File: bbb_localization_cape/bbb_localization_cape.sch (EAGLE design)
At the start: 33 parts, among them J2 MOLEX-22-03-5035, U1 SN65HVD256DR, U2 ARDUCAMOV5642, U3 SN74LV1T126DCKR, U4 MSP430G2553IPW20R, U5 SN74LV1T125DCKR, U6 LP38693MP-3.3/NOPB, U7 LM1085ISX-ADJ

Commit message: Went over the entire schematic
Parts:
- removed C1: 100nF, resistor:C-USC1206
- removed R3: 47k, resistor:R-US_R1206
- J2: device bbb_cape_parts:MOLEX-22-03-5035 -> bbb_localization_cape:MOLEX-22-03-5035
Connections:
- removed net N$7: C1.1, R3.1, U4.P1.3/ADC10CLK/CAOUT/VREF-/VEREF-/A3/CA3
- net +3V3: no longer R3.2
- net GND: no longer C1.2
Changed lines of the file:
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@@
 <setting verticaltext="up"/>
 </settings>
-<grid distance="0.1" unitdist="inch" unit="inch" style="lines" multiple="1" display="yes" altdistance="0.01" altunitdist="inch" altunit="inch"/>
+<grid distance="0.1" unitdist="inch" unit="inch" style="lines" multiple="1" display="no" altdistance="0.01" altunitdist="inch" altunit="inch"/>
 <layers>
 <layer number="1" name="Top" color="4" fill="1" visible="no" active="no"/>
@@
 <part name="U4" library="bbb_cape_parts" deviceset="MSP430G2553IPW20R" device=""/>
 <part name="+3V35" library="supply1" library_urn="urn:adsk.eagle:library:371" deviceset="+3V3" device=""/>
-<part name="R3" library="resistor" library_urn="urn:adsk.eagle:library:348" deviceset="R-US_" device="R1206" package3d_urn="urn:adsk.eagle:package:26062/1" value="47k"/>
-<part name="C1" library="resistor" library_urn="urn:adsk.eagle:library:348" deviceset="C-US" device="C1206" package3d_urn="urn:adsk.eagle:package:26140/1" value="100nF"/>
-<part name="GND3" library="supply1" library_urn="urn:adsk.eagle:library:371" deviceset="GND" device=""/>
 <part name="+3V37" library="supply1" library_urn="urn:adsk.eagle:library:371" deviceset="+3V3" device=""/>
 <part name="R5" library="resistor" library_urn="urn:adsk.eagle:library:348" deviceset="R-US_" device="R1206" package3d_urn="urn:adsk.eagle:package:26062/1" value="47k"/>
@@
 <part name="R4" library="resistor" library_urn="urn:adsk.eagle:library:348" deviceset="R-US_" device="R1206" package3d_urn="urn:adsk.eagle:package:26062/1" value="10k"/>
 <part name="P+4" library="supply1" library_urn="urn:adsk.eagle:library:371" deviceset="+5V" device=""/>
-<part name="J2" library="bbb_cape_parts" deviceset="MOLEX-22-03-5035" device=""/>
+<part name="J2" library="bbb_localization_cape" deviceset="MOLEX-22-03-5035" device=""/>
 <part name="GND6" library="supply1" library_urn="urn:adsk.eagle:library:371" deviceset="GND" device=""/>
 <part name="SUPPLY1" library="supply2" library_urn="urn:adsk.eagle:library:372" deviceset="+10V" device=""/>
@@
 <attribute name="VALUE" x="65.7606" y="92.9386" size="2.0828" layer="96" ratio="6" rot="SR0"/>
 </instance>
-<instance part="+3V35" gate="G$1" x="20.32" y="96.52" smashed="yes">
-<attribute name="VALUE" x="20.32" y="96.52" size="1.778" layer="96"/>
-</instance>
-<instance part="R3" gate="G$1" x="20.32" y="83.82" smashed="yes" rot="R90">
-<attribute name="NAME" x="23.9014" y="85.09" size="1.778" layer="95"/>
-<attribute name="VALUE" x="23.622" y="82.55" size="1.778" layer="96"/>
-</instance>
-<instance part="C1" gate="G$1" x="20.32" y="71.12" smashed="yes">
-<attribute name="NAME" x="23.876" y="69.215" size="1.778" layer="95"/>
-<attribute name="VALUE" x="23.876" y="66.929" size="1.778" layer="96"/>
-</instance>
-<instance part="GND3" gate="1" x="20.32" y="60.96"/>
+<instance part="+3V35" gate="G$1" x="55.88" y="91.44" smashed="yes">
+<attribute name="VALUE" x="55.88" y="91.44" size="1.778" layer="96"/>
+</instance>
 <instance part="+3V37" gate="G$1" x="256.54" y="93.98" smashed="yes">
 <attribute name="VALUE" x="256.54" y="93.98" size="1.778" layer="96"/>
@@
 </busses>
 <nets>
-<net name="N$7" class="0">
-<segment>
-<pinref part="R3" gate="G$1" pin="1"/>
-<wire x1="20.32" y1="78.74" x2="20.32" y2="76.2" width="0.1524" layer="91"/>
-<pinref part="U4" gate="A" pin="P1.3/ADC10CLK/CAOUT/VREF-/VEREF-/A3/CA3"/>
-<wire x1="20.32" y1="76.2" x2="58.42" y2="76.2" width="0.1524" layer="91"/>
-<pinref part="C1" gate="G$1" pin="1"/>
-<wire x1="20.32" y1="73.66" x2="20.32" y2="76.2" width="0.1524" layer="91"/>
-<junction x="20.32" y="76.2"/>
-</segment>
-</net>
 <net name="+3V3" class="0">
 <segment>
 <pinref part="+3V35" gate="G$1" pin="+3V3"/>
-<pinref part="R3" gate="G$1" pin="2"/>
-<wire x1="20.32" y1="93.98" x2="20.32" y2="91.44" width="0.1524" layer="91"/>
+<wire x1="55.88" y1="88.9" x2="55.88" y2="86.36" width="0.1524" layer="91"/>
 <pinref part="U4" gate="A" pin="DVCC"/>
-<wire x1="20.32" y1="91.44" x2="20.32" y2="88.9" width="0.1524" layer="91"/>
-<wire x1="58.42" y1="86.36" x2="35.56" y2="86.36" width="0.1524" layer="91"/>
-<wire x1="35.56" y1="86.36" x2="35.56" y2="91.44" width="0.1524" layer="91"/>
-<wire x1="20.32" y1="91.44" x2="35.56" y2="91.44" width="0.1524" layer="91"/>
-<junction x="20.32" y="91.44"/>
+<wire x1="58.42" y1="86.36" x2="55.88" y2="86.36" width="0.1524" layer="91"/>
 </segment>
 <segment>
@@
 <net name="GND" class="0">
 <segment>
-<pinref part="C1" gate="G$1" pin="2"/>
-<pinref part="GND3" gate="1" pin="GND"/>
-<wire x1="20.32" y1="66.04" x2="20.32" y2="63.5" width="0.1524" layer="91"/>
-</segment>
-<segment>
 <pinref part="U4" gate="A" pin="DVSS"/>

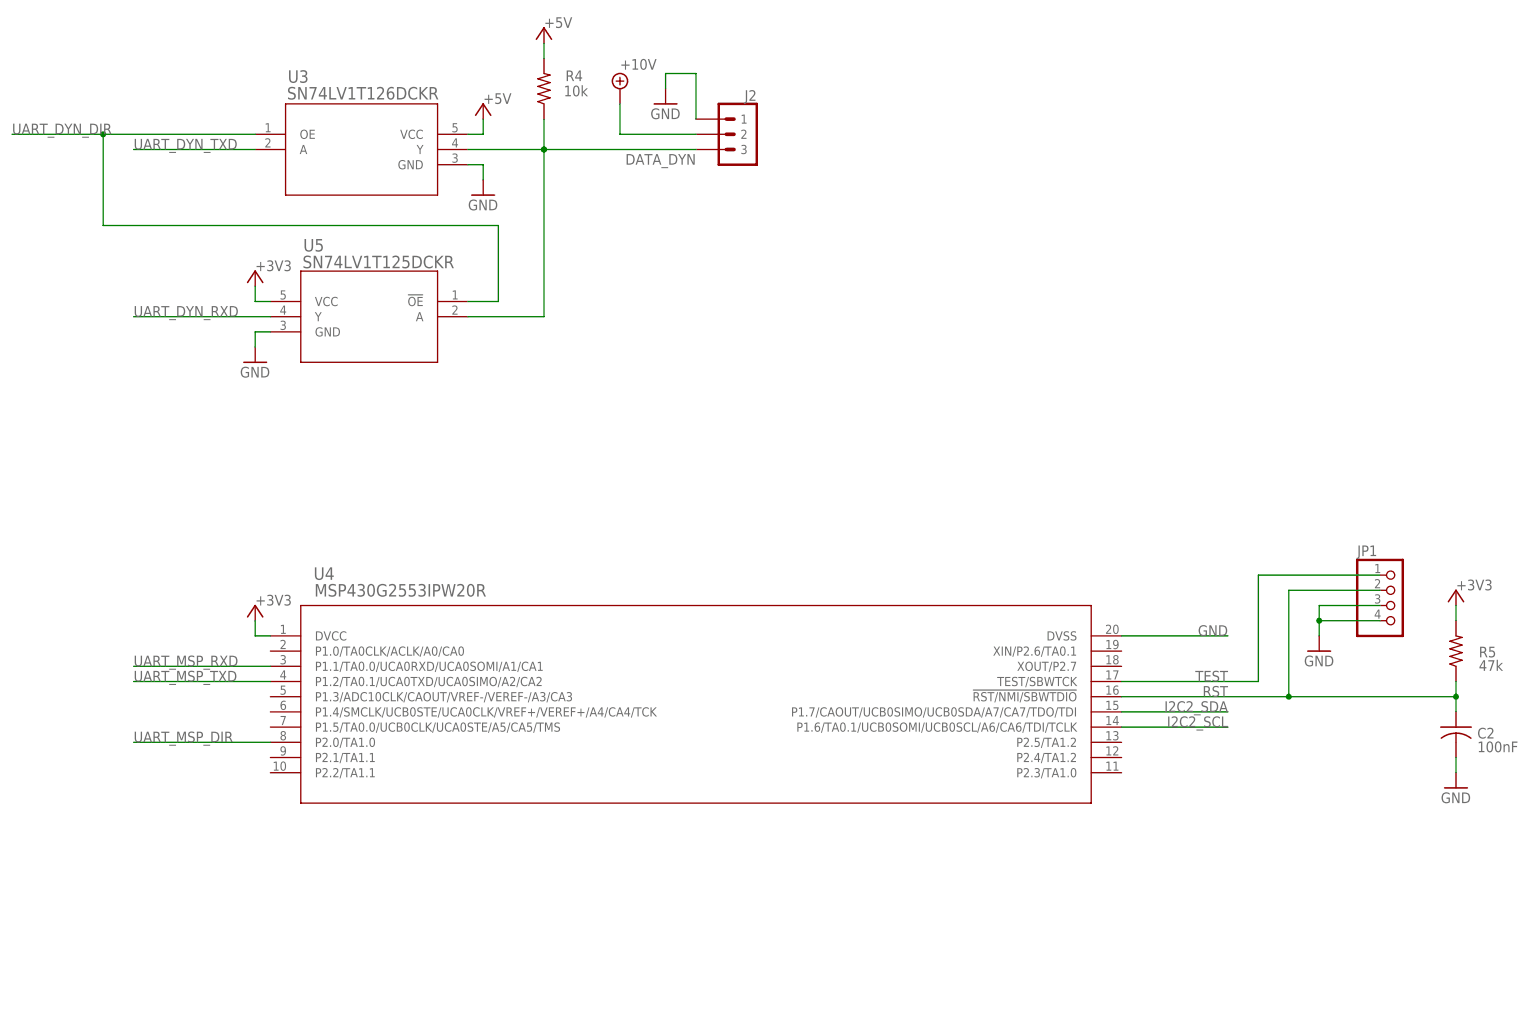
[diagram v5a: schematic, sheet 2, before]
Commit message: Added components to deal with voltages during poweroff
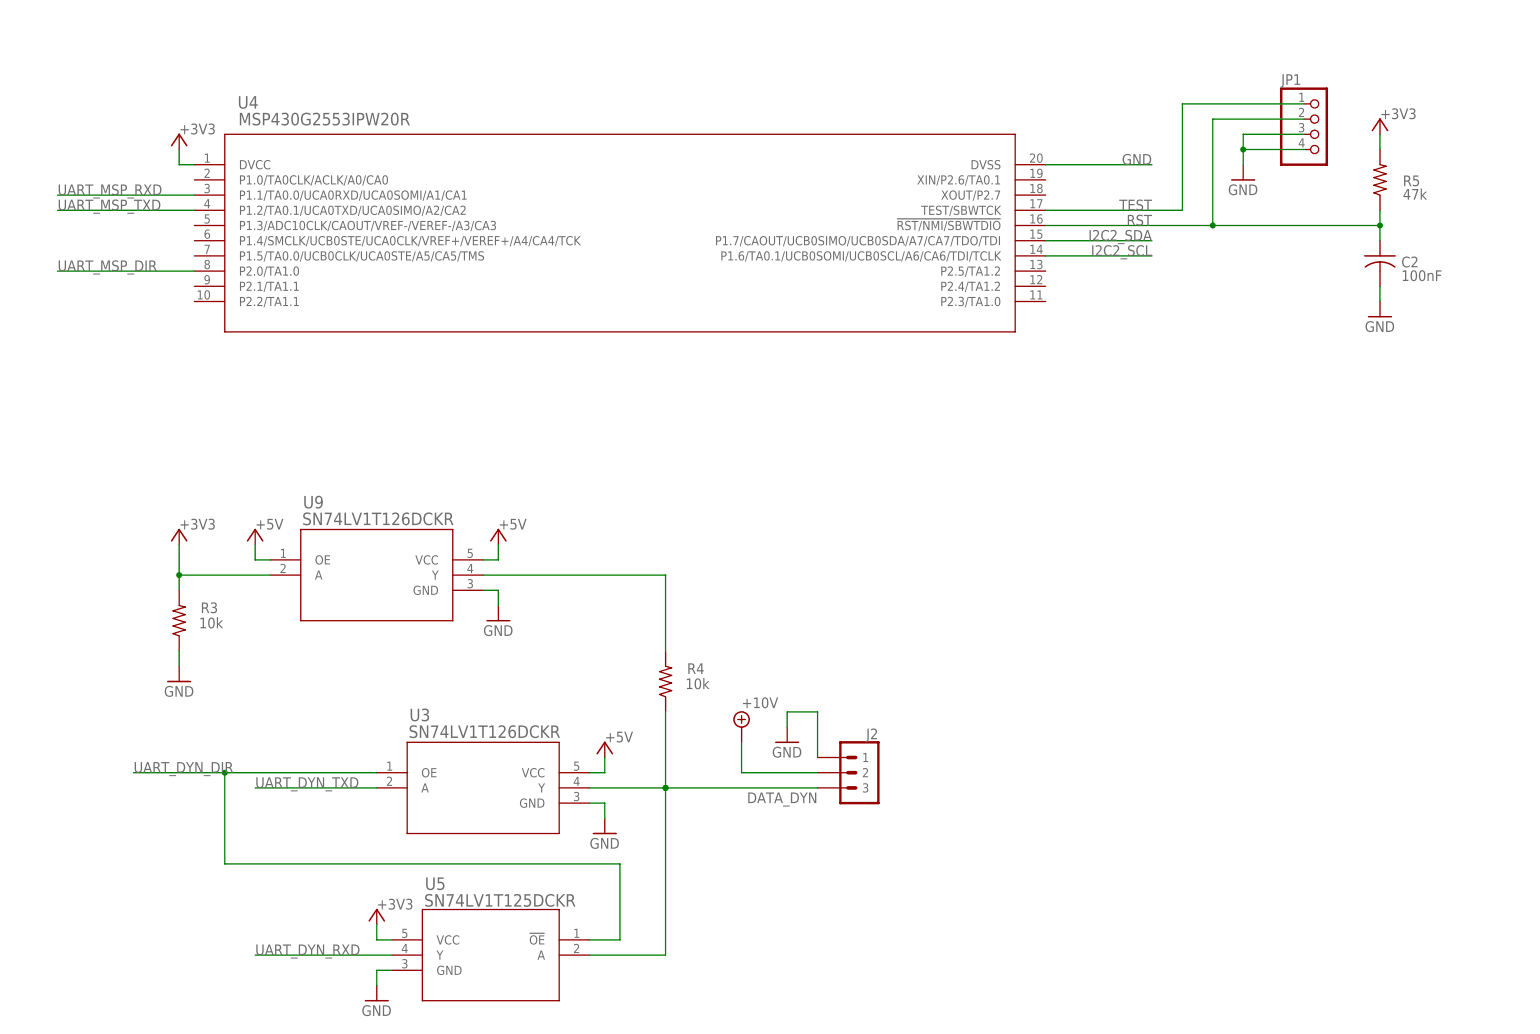
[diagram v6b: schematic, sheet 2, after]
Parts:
- added R3: 10k, resistor:R-US_R1206
- added U8, U9: SN74LV1T126DCKR, bbb_localization_cape:SN74LV1T126DCKR
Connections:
- new net N$4: R4.2, U9.Y
- new net N$5: U6.VEN, U8.Y
- new net SYS_RESETN: A1.SYS_RESETN.10@P9, U8.A
- net +3V3: now also R3.2, U8.OE, U9.A
- net +5V: now also U8.VCC, U9.OE, U9.VCC; no longer R4.2, U6.VEN
- net GND: now also R3.1, U8.GND, U9.GND
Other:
- moved on the sheet: +12V, C2, C4, C7, C8, GND, J2, JP1, R4, R5, U3, U4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

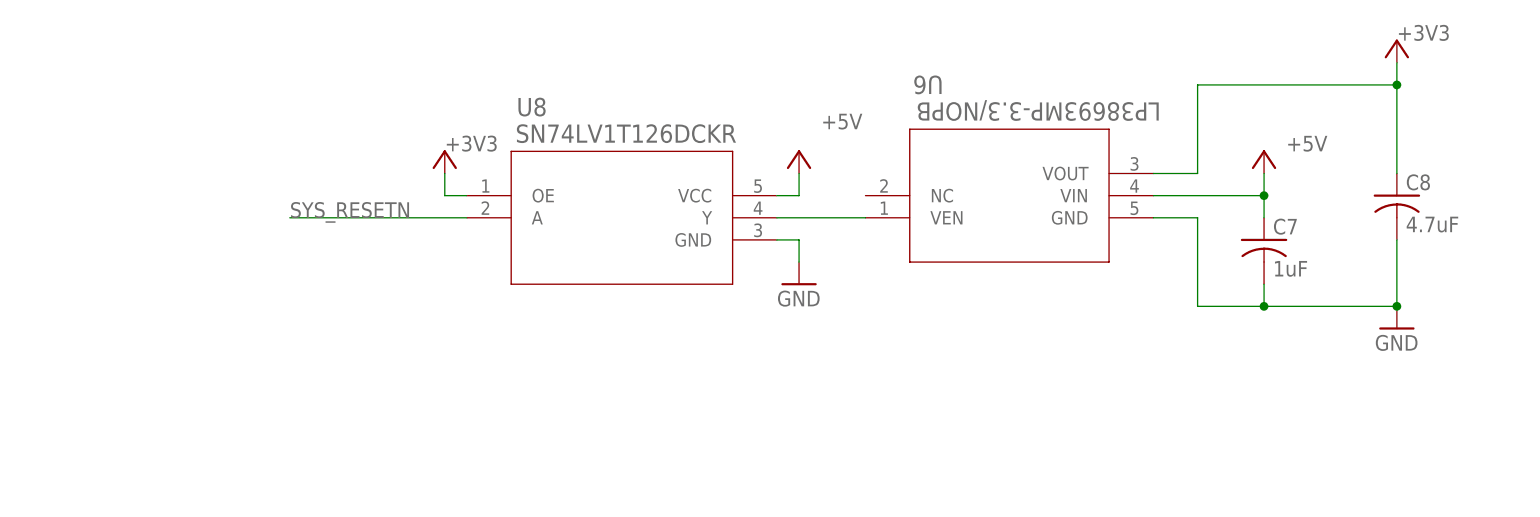
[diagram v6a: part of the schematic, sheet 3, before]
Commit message: Consolidated powerdown level shifters from 2 to 1
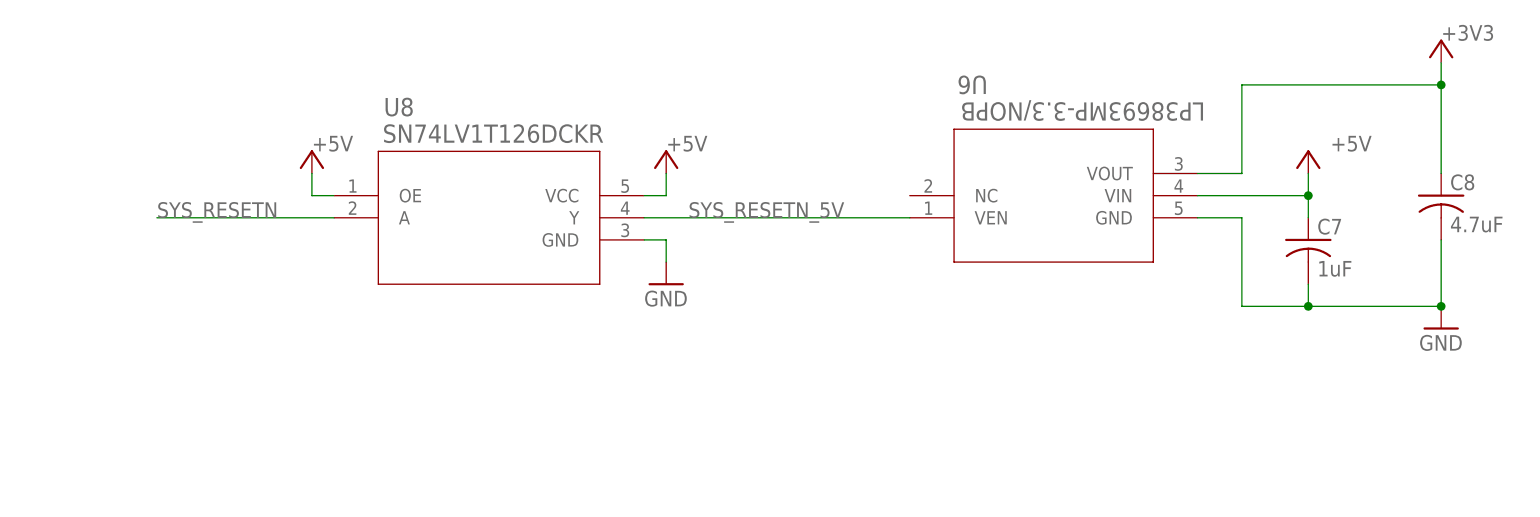
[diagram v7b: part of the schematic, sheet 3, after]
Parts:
- removed R3: 10k, resistor:R-US_R1206
- removed U9: SN74LV1T126DCKR, bbb_localization_cape:SN74LV1T126DCKR
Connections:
- removed net N$4: R4.2, U9.Y
- removed net N$5: U6.VEN, U8.Y
- new net SYS_RESETN_5V: R4.2, U6.VEN, U8.Y
- net +3V3: no longer R3.2, U8.OE, U9.A
- net +5V: now also U8.OE; no longer U9.OE, U9.VCC
- net GND: no longer R3.1, U9.GND
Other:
- moved on the sheet: C7, C8, R4, U6, U8

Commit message: Added 10V and 5V lines
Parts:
- C3, C5: device resistor:C-USC1206 -> resistor:C-USC0805
- R6, R7: device resistor:R-US_R1206 -> resistor:R-US_R0805
